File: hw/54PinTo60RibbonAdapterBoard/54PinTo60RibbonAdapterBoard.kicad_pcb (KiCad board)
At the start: 2 copper layers, 72 x 23 mm, 2 parts, among them J1 Conn_02x27_Odd_Even, J2 Conn_01x60_Pin

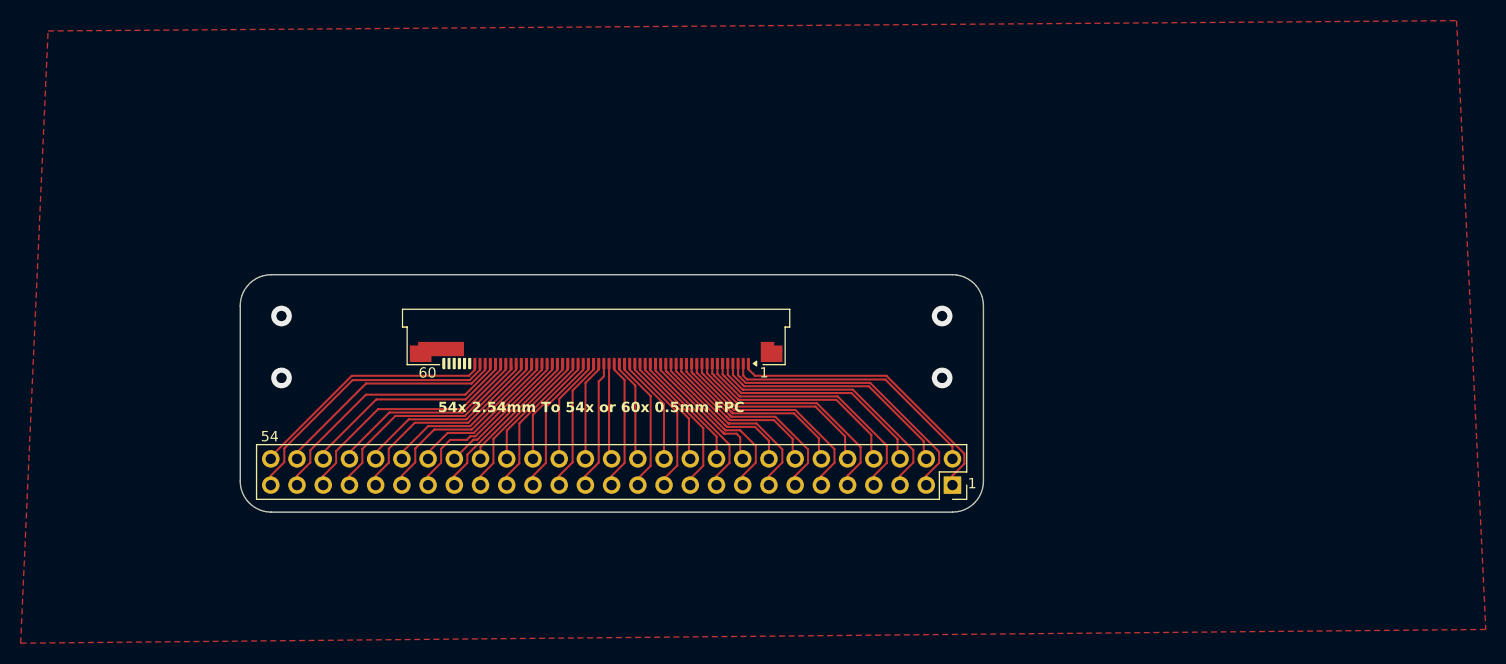
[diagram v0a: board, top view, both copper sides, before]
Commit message: Updated FPC connector on 54 Pin Adapter Board
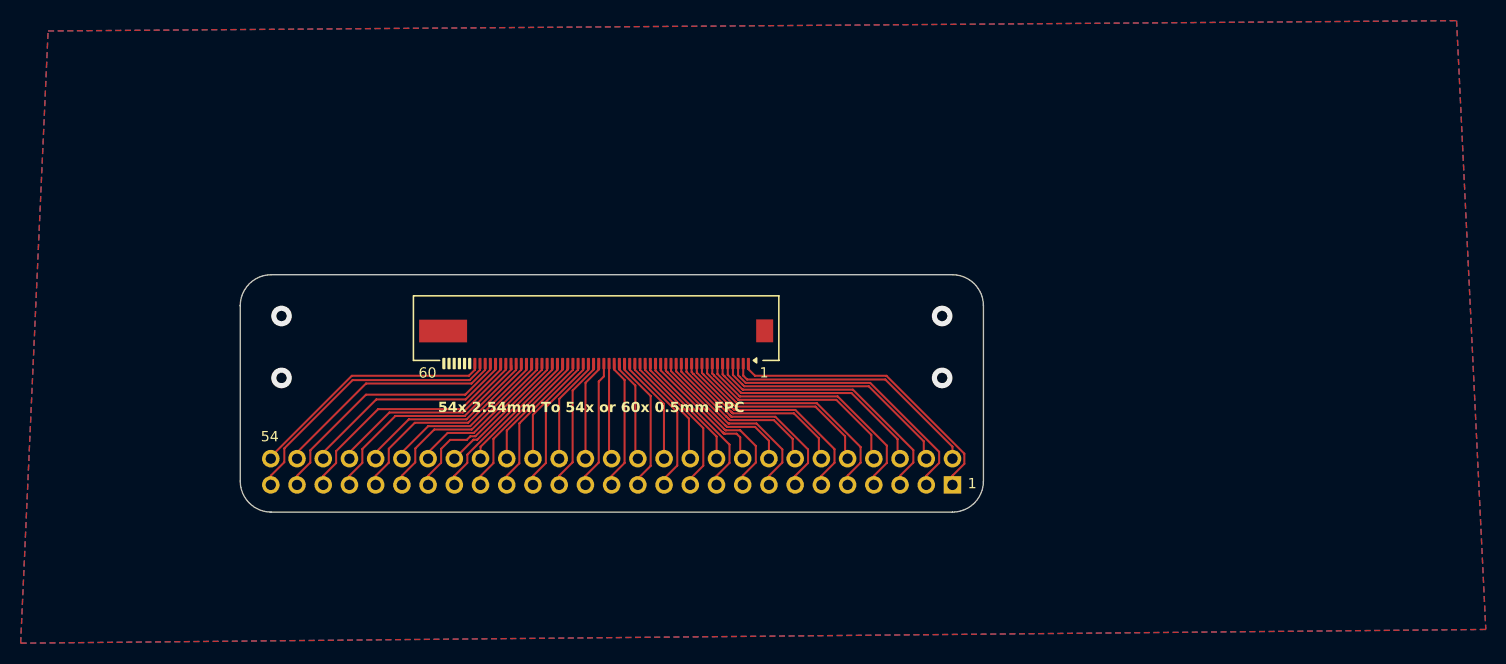
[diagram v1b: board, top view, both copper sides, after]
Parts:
- J1: moved to B.Cu
- J2: footprint Connector_FFC-FPC:Amphenol_F32R-1A7x1-11060_1x60-1MP_P0.5mm_Horizontal -> gg_lcd:1x54 To 1x60 FPC Connector 0.5mm
- moved J1 3.36 mm to (170.0, 120.4), turned to 90 degrees
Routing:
- added copper zone on B.Cu, net GND

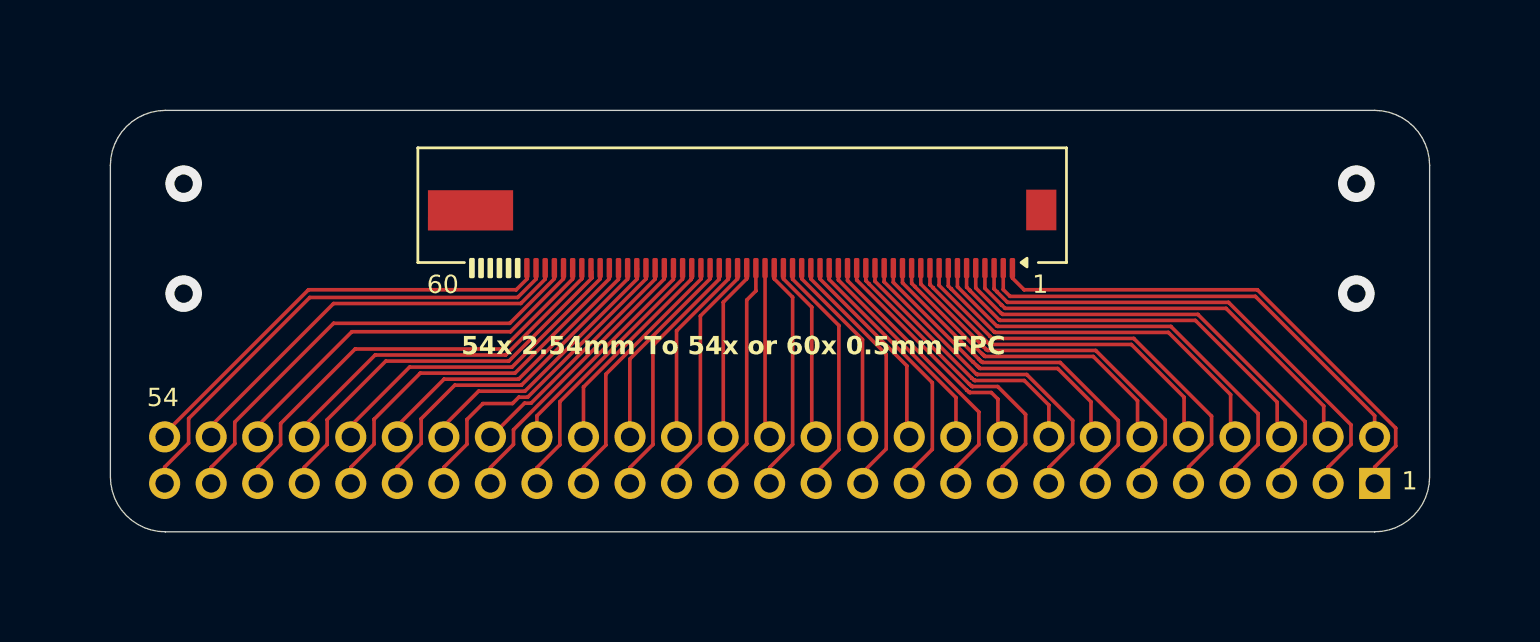
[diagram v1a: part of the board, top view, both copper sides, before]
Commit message: Updated pin assignments on main PCB to match pico code using the correct sequential pins.
54PinTo60RibbonAdapterBoard tweaked trace layout to reduce overall board size slightly.
Added InstallationFlexWithSolderPoints for installing without a ribbon connector.
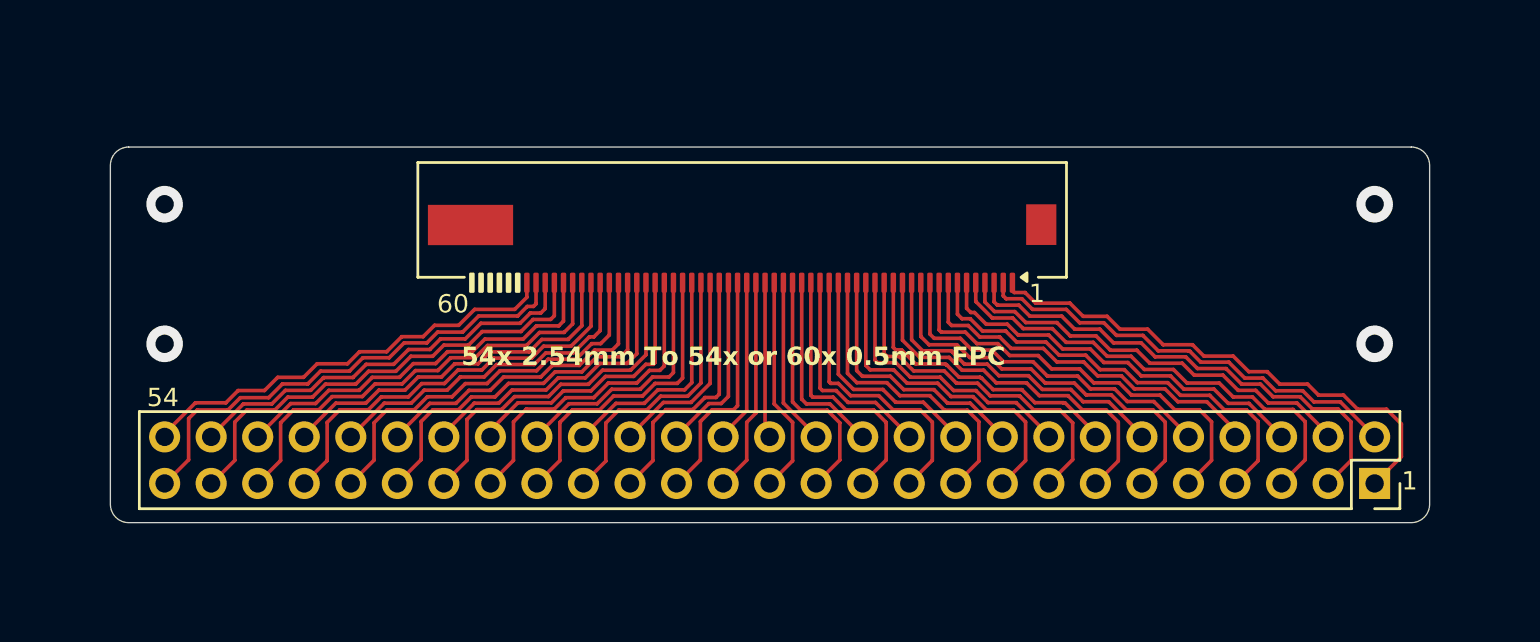
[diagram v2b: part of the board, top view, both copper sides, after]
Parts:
- moved J2 0.80 mm to (135.5, 106.5)
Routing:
- net Net-(J1-Pin_39): track 15.7 -> 17.9 mm
- net Net-(J1-Pin_40): track 13.2 -> 15.3 mm
- net Net-(J1-Pin_18): track 12.8 -> 14.8 mm
- net Net-(J1-Pin_19): track 15.3 -> 17.1 mm
- net Net-(J1-Pin_37): track 15.1 -> 16.8 mm
- net Net-(J1-Pin_17): track 16.8 -> 18.4 mm
- net Net-(J1-Pin_41): track 17.6 -> 19.2 mm
- net Net-(J1-Pin_2): track 26.0 -> 24.4 mm
- net Net-(J1-Pin_38): track 12.5 -> 14.0 mm
- net Net-(J1-Pin_42): track 14.9 -> 16.4 mm
- net Net-(J1-Pin_21): track 14.4 -> 15.8 mm
- net Net-(J1-Pin_15): track 18.2 -> 19.6 mm
- net Net-(J1-Pin_14): track 15.8 -> 17.2 mm
- net Net-(J1-Pin_20): track 11.3 -> 12.6 mm
- net Net-(J1-Pin_44): track 16.4 -> 17.6 mm
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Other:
- board size 72 x 23 mm -> 72 x 20.5 mm

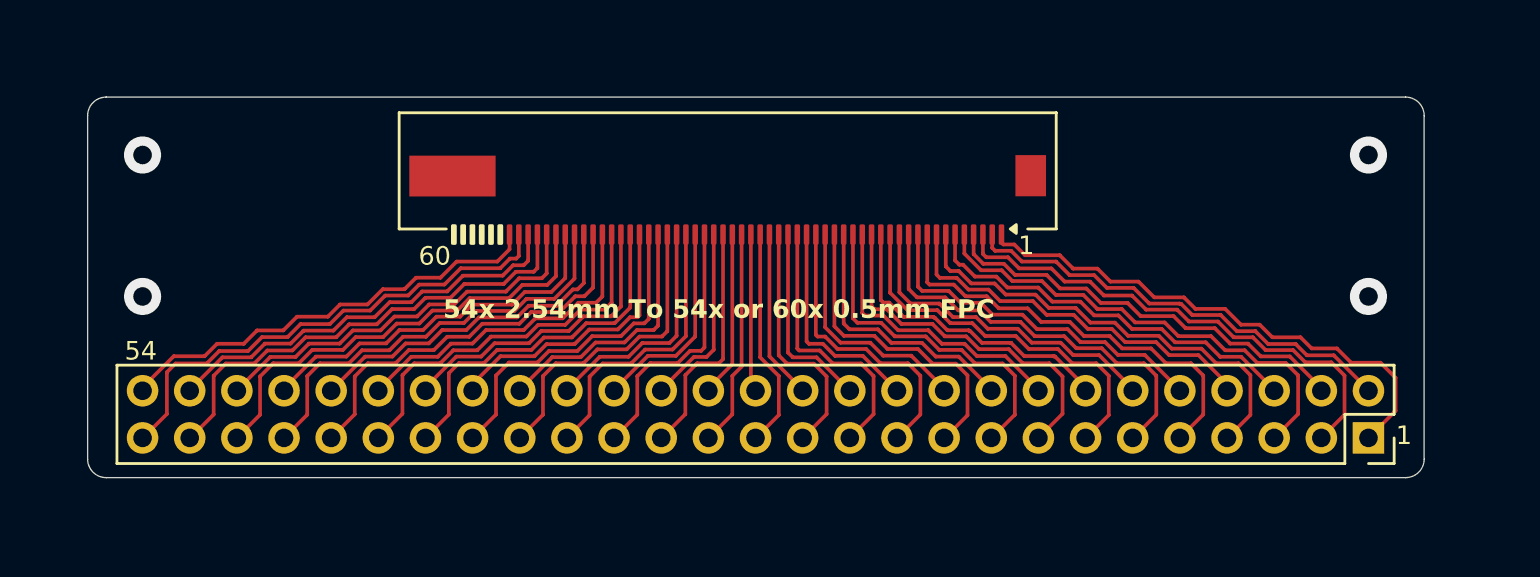
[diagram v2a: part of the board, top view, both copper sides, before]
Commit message: Updated 54/60 Pin FPC connector footprint.
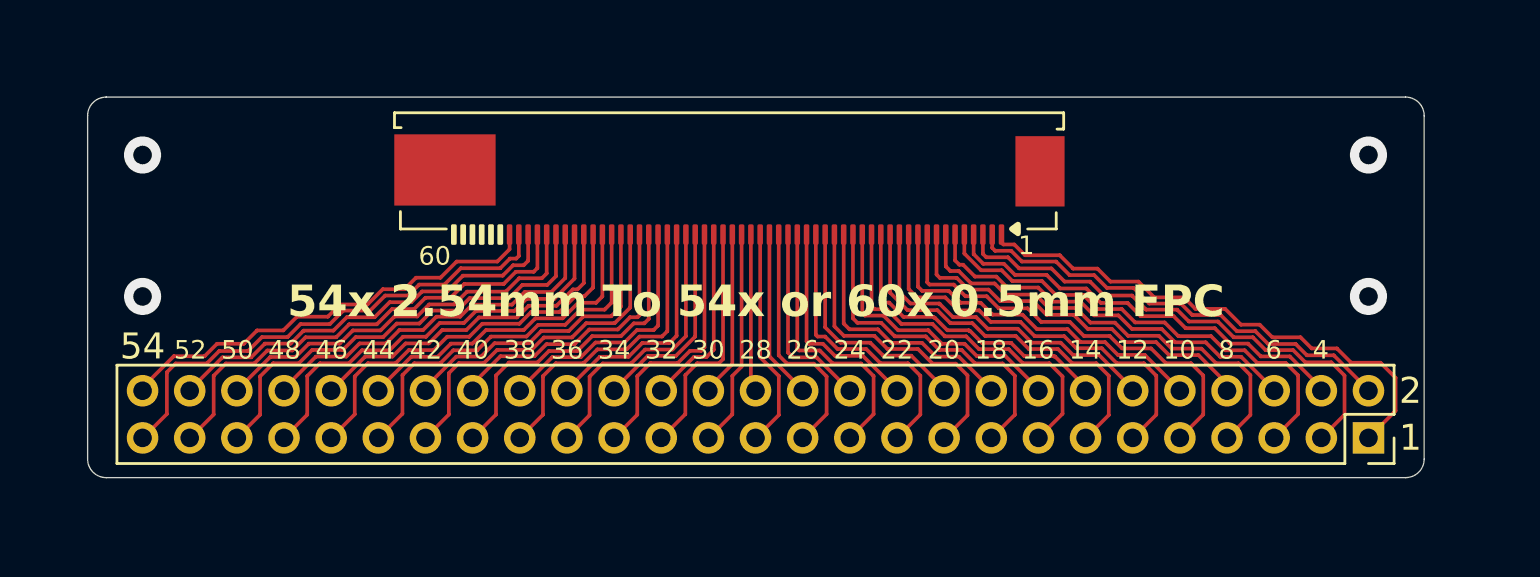
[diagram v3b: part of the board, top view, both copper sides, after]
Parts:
- J2: footprint gg_lcd:1x54 To 1x60 FPC Connector 0.5mm -> gg_lcd:1x54 To 1x60 FPC Connector 0.5mm HandSolder
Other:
- board text added: "10"
- board text added: "12"
- board text added: "14"
- board text added: "16"
- board text added: "18"
- board text added: "2"
- board text added: "20"
- board text added: "22"
- board text added: "24"
- board text added: "26"
- board text added: "28"
- board text added: "30"
- board text added: "32"
- board text added: "34"
- board text added: "36"
- board text added: "38"
- board text added: "4"
- board text added: "40"
- board text added: "42"
- board text added: "44"
- board text added: "46"
- board text added: "48"
- board text added: "50"
- board text added: "52"
- board text added: "6"
- board text added: "8"
